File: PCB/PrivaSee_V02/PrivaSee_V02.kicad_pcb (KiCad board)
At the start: 4 copper layers, 69.8 x 90 mm, 31 parts, among them J1 RFPC-SMA27-F, J2 Batt_Solder_Point, J3 Conn_02x06_Odd_Even, SW1 Switch, SW2 SW_Push, U2 LM358, U3 254, U4 DFR0568, U6 ESP32-C5-DevKitC-1

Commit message: Fixed PCB Improt
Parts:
- moved G*** 3.64 mm to (84.5, 39.0)
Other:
- board text added: "Privasee"
- board text added: "V 1.0"
- board text added: "https://github.com/OSHE-Github/Privasee"

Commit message: Apply .gitignore to stop tracking ignored files
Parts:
- moved ? 2.55 mm to (85.0, 41.5)
- renumbered G*** to ?
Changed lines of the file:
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@@
 	(footprint "LOGO"
 		(layer "F.Cu")
-		(at 84.5 39)
-		(property "Reference" "G***"
+		(at 85 41.5)
+		(property "Reference" ""
 			(at 0 0 0)
 			(layer "F.SilkS")

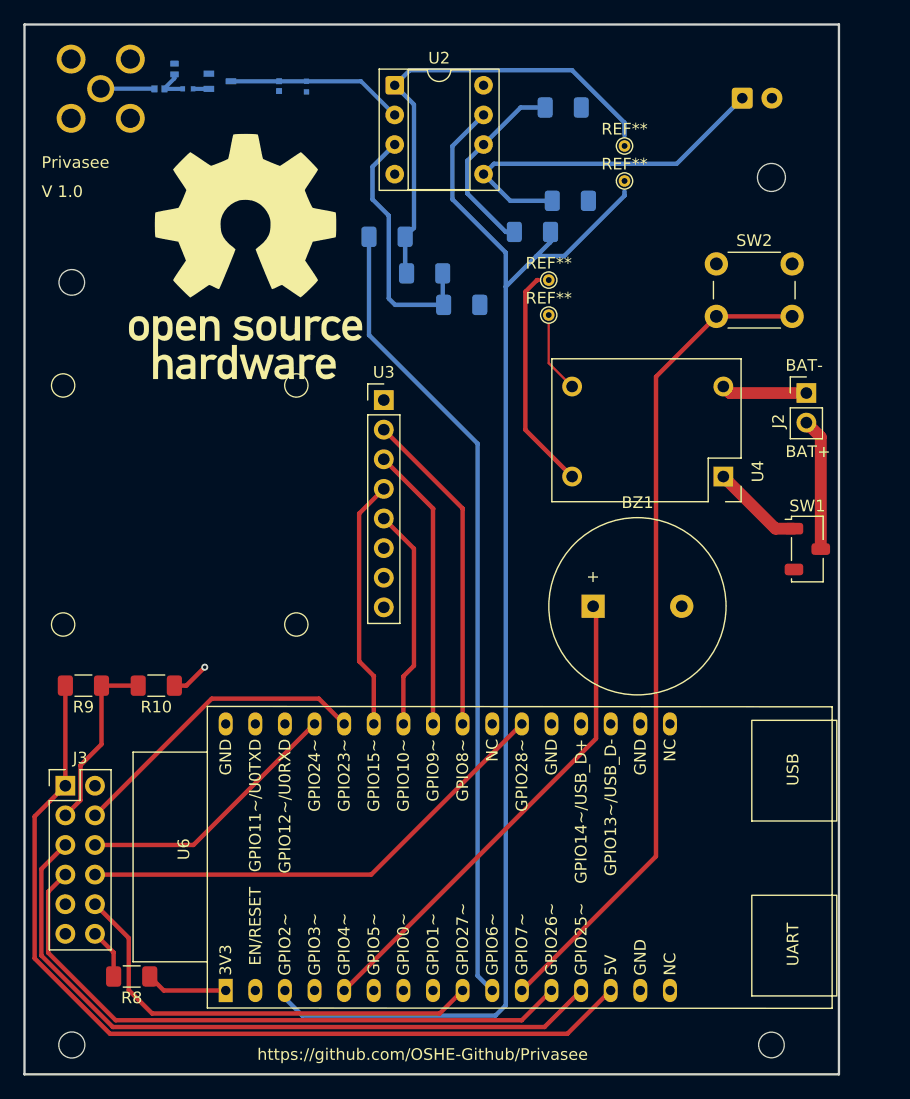
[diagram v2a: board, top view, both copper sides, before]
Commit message: PCB appearance updates
Updates to the silkscreen, footprint labels, and test points added
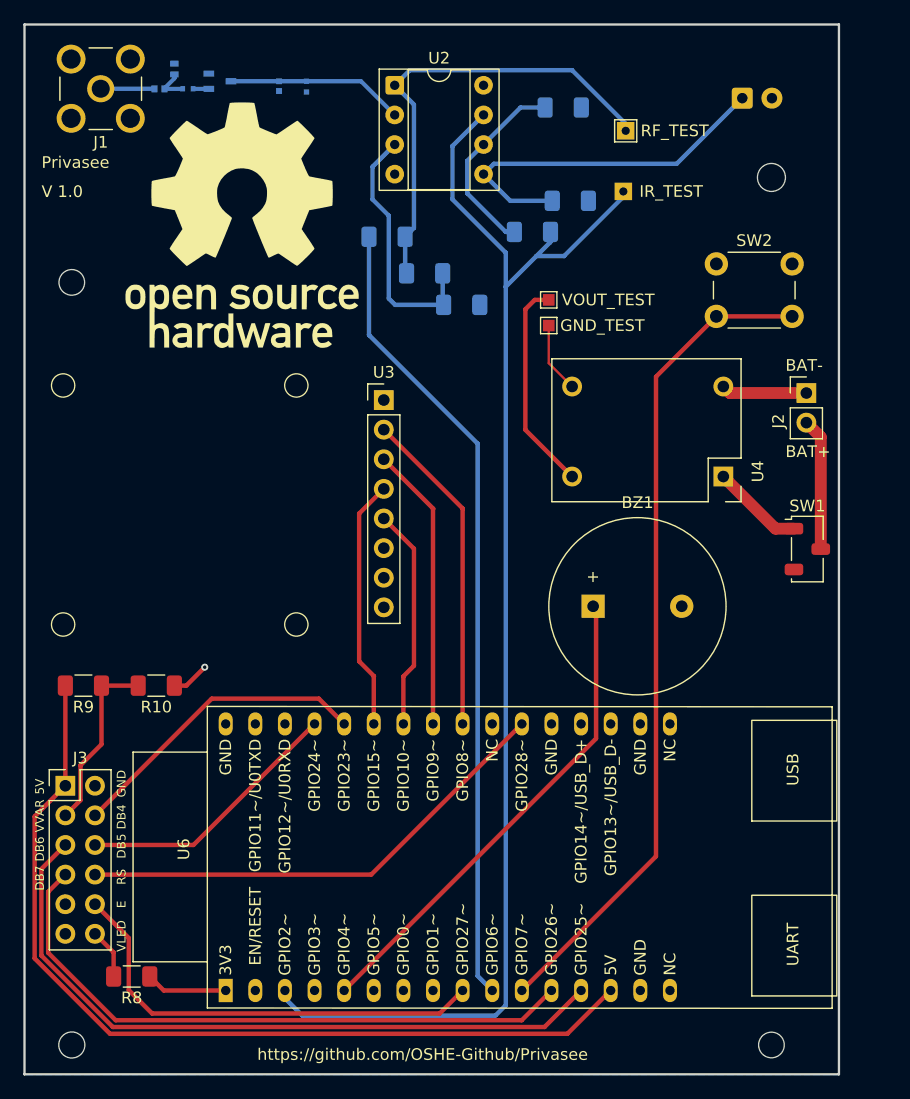
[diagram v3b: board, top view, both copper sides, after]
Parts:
- removed REF**: RF_TESTPOINT, TestPoint:TestPoint_THTPad_D1.0mm_Drill0.5mm
- removed REF**: GND_TESTPOINT, TestPoint:TestPoint_THTPad_D1.0mm_Drill0.5mm
- removed REF**: Vin_TESTPOINT, TestPoint:TestPoint_THTPad_D1.0mm_Drill0.5mm
- removed REF**: IR_TESTPOINT, TestPoint:TestPoint_THTPad_D1.0mm_Drill0.5mm
- added J4: VOUT_TEST, TestPoint:TestPoint_Pad_1.0x1.0mm, F.Cu at (111.0, 45.2)
- added J5: GND_TEST, TestPoint:TestPoint_Pad_1.0x1.0mm, F.Cu at (111.0, 47.4)
- added J6: IR_TEST, TestPoint:TestPoint_THTPad_1.5x1.5mm_Drill0.7mm, B.Cu at (117.4, 35.9)
- added J7: RF_TEST, TestPoint:TestPoint_THTPad_1.5x1.5mm_Drill0.7mm, F.Cu at (117.6, 30.7)
- J1: moved to F.Cu
- moved ? 2.72 mm to (84.7, 38.8)
- turned J1 to -90 degrees
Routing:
- net /3V3: track 140.6 -> 139.9 mm

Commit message: Stackup/RF Changes
Reassessed layer stackup. RF components are implemented/positioned correctly. Added values to passive RF components.
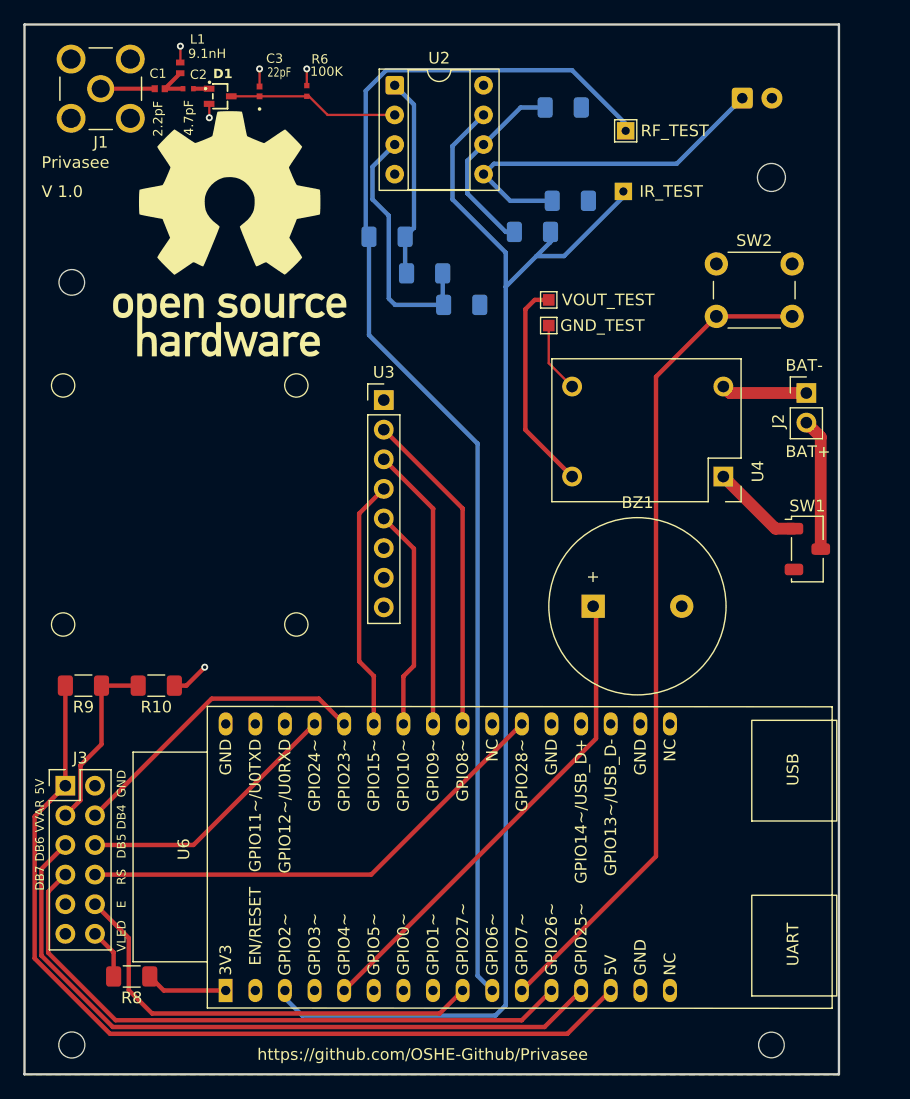
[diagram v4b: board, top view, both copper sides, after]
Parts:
- C1, C2, C3, D1, L1, R6: moved to F.Cu
- moved C3 1.73 mm to (86.2, 27.3), turned to 90 degrees
- moved ? 1.30 mm to (83.6, 39.5)
- moved D1 1.29 mm to (82.8, 27.7)
- moved L1 0.51 mm to (79.4, 25.3)
- moved R6 0.37 mm to (90.2, 27.3), turned to -90 degrees
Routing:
- net Net-(J7-Pin_1): track 69.0 -> 107.6 mm
- net Net-(R1-Pad2): track 40.4 -> 17.2 mm
- net GND: track 9.42 -> 15.0 mm, vias 1 -> 5
- net Net-(D1-C/A): track 15.5 -> 15.0 mm
- added copper zone on F.Cu, net (none)
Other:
- board text added: "100K"
- board text added: "2.2pF"
- board text added: "22pF"
- board text added: "4.7pF"
- board text added: "9.1nH"
- board text added: "D1"

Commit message: Removed Top Layer Ground Pour
I dont think this is needed and I think this may degrade signal performance for RF
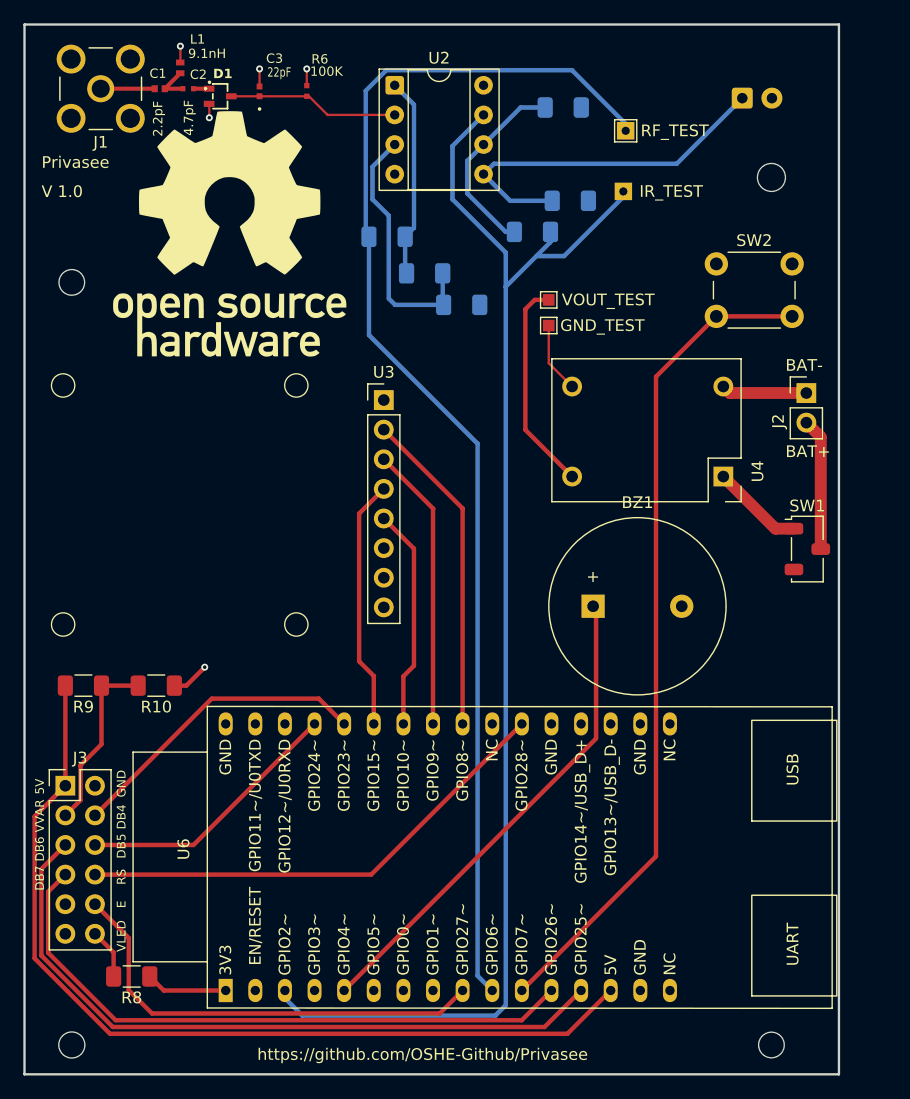
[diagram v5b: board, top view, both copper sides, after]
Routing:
- removed copper zone on F.Cu, net (none)
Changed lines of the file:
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@@
-	)
-	(zone
-		(layer "F.Cu")
-		(name "Signal")
-		(hatch edge 0.5)
-		(priority 1)
-		(connect_pads
-			(clearance 0.5)
-		)
-		(min_thickness 0.25)
-		(fill yes
-			(thermal_gap 0.5)
-			(thermal_bridge_width 0.5)
-			(island_removal_mode 1)
-		)
-		(polygon
-			(pts
-				(xy 135.89 21.59) (xy 135.89 111.64) (xy 66.04 111.63) (xy 66.04 21.59)
-			)
-		)
 	)
 	(zone

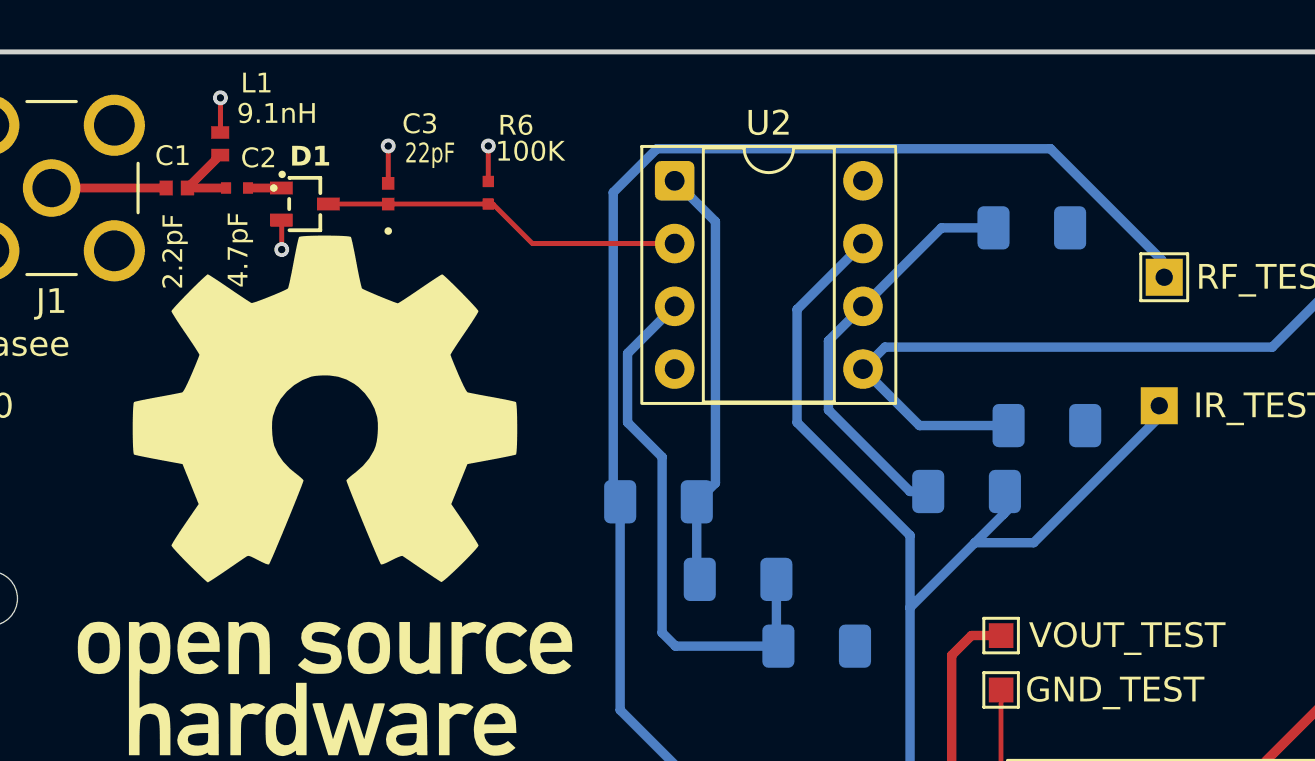
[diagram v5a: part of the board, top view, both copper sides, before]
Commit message: Minor Changes
Removed traces that are connected via 3v3 net. Removed acute angle at L1. Adjusted spacing near LM358 power.
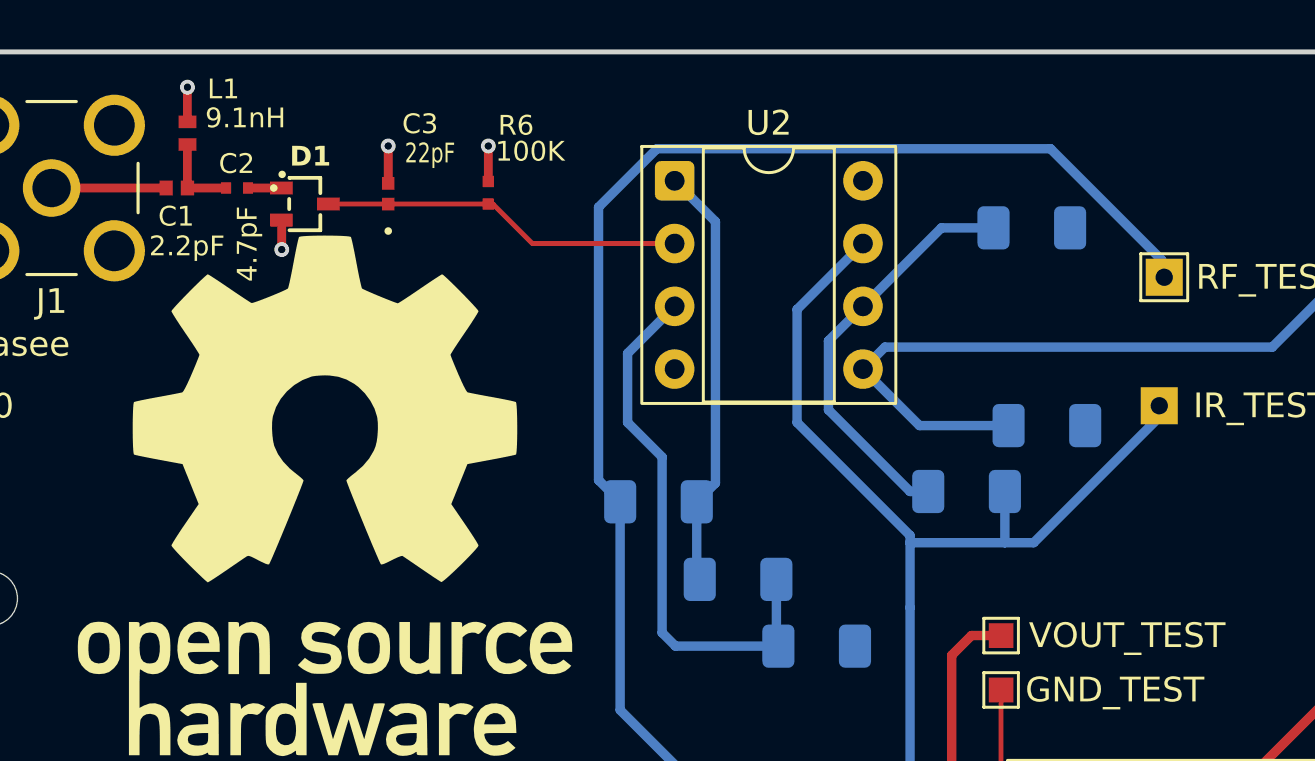
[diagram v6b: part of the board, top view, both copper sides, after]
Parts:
- moved L1 1.39 mm to (78.1, 24.9)
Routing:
- net /3V3: track 139.9 -> 25.4 mm
- net Net-(J6-Pin_1): track 116.5 -> 114.7 mm
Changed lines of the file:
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@@
 		(tags "GJM1555C1H4R7CB01D ")
 		(property "Reference" "C2"
-			(at -0.877216 1.2082 0)
+			(at 0.012784 0.9782 0)
 			(unlocked yes)
 			(layer "F.SilkS")
@@
 	(footprint "Snapeda:INDC1006X60N"
 		(layer "F.Cu")
-		(at 79.4 25.3 -90)
+		(at 78.075 24.87 -90)
 		(property "Reference" "L1"
-			(at -2.45 -1.48 0)
+			(at -1.78 -1.455 0)
 			(layer "F.SilkS")
 			(effects
@@
 		(at 77.643 27.0882 180)
 		(property "Reference" "C1"
-			(at 0.153 1.2982 180)
+			(at 0.023 -1.1518 180)
 			(layer "F.SilkS")
 			(effects
@@
 		)
 	)
-	(gr_text "9.1nH"
-		(at 80.07 24.55 0)
+	(gr_text "2.2pF"
+		(at 76.52 29.91 0)
 		(layer "F.SilkS")
 		(effects
@@
 		)
 	)
-	(gr_text "100K"
-		(at 90.53 26.08 0)
+	(gr_text "9.1nH"
+		(at 78.79 24.73 0)
 		(layer "F.SilkS")
 		(effects
@@
 		)
 	)
-	(gr_text "2.2pF"
-		(at 77.96 31.2 90)
+	(gr_text "100K"
+		(at 90.53 26.08 0)
 		(layer "F.SilkS")
 		(effects
@@
 	)
 	(gr_text "4.7pF"
-		(at 80.6 31.13 90)
+		(at 80.97 30.89 90)
 		(layer "F.SilkS")
 		(effects
@@
 	)
 	(segment
-		(start 78.075 27.085)
-		(end 79.4 25.76)
-		(width 0.355476)
-		(layer "F.Cu")
-		(net "Net-(C1-Pad1)")
-	)
-	(segment
 		(start 78.075 27.0882)
-		(end 79.638284 27.0882)
+		(end 78.075 25.33)
 		(width 0.355476)
 		(layer "F.Cu")
@@
 	(segment
 		(start 78.075 27.0882)
-		(end 78.075 27.085)
+		(end 79.638284 27.0882)
 		(width 0.355476)
 		(layer "F.Cu")
@@
 		(start 86.2 25.39)
 		(end 86.2 26.9)
-		(width 0.2)
+		(width 0.355476)
 		(layer "F.Cu")
 		(net "GND")
@@
 		(start 81.89 29.58)
 		(end 81.89 28.400916)
-		(width 0.2)
+		(width 0.355476)
 		(layer "F.Cu")
 		(net "GND")
@@
 	)
 	(segment
-		(start 79.41 24.83)
-		(end 79.4 24.84)
+		(start 78.08 24.4)
+		(end 78.07 24.41)
 		(width 0.2)
 		(layer "F.Cu")
@@
 		(start 90.25 25.39)
 		(end 90.25 26.8238)
-		(width 0.2)
+		(width 0.355476)
 		(layer "F.Cu")
 		(net "GND")
 	)
 	(segment
-		(start 79.41 23.44)
-		(end 79.41 24.83)
-		(width 0.2)
+		(start 78.075 23.01)
+		(end 78.075 24.4)
+		(width 0.355476)
 		(layer "F.Cu")
 		(net "GND")
@@
 	)
 	(via
-		(at 79.41 23.44)
+		(at 78.075 23.01)
 		(size 0.6)
 		(drill 0.3)
@@
 	)
 	(segment
-		(start 113.005 60.35)
-		(end 116.9 56.455)
-		(width 0.381)
-		(layer "In2.Cu")
-		(net "/3V3")
-	)
-	(segment
-		(start 113.005 60.35)
-		(end 109.9 63.455)
-		(width 0.381)
-		(layer "In2.Cu")
-		(net "/3V3")
-	)
-	(segment
-		(start 109.9 63.455)
-		(end 109.9 82.9)
-		(width 0.381)
-		(layer "In2.Cu")
-		(net "/3V3")
-	)
-	(segment
-		(start 116.9 56.455)
-		(end 116.9 53.527)
-		(width 0.381)
-		(layer "In2.Cu")
-		(net "/3V3")
-	)
-	(segment
-		(start 104.765496 82.957331)
-		(end 83.295996 104.426831)
-		(width 0.381)
-		(layer "In2.Cu")
-		(net "/3V3")
-	)
-	(segment
-		(start 104.3262 69.0288)
-		(end 96.8548 69.0288)
-		(width 0.381)
-		(layer "In2.Cu")
-		(net "/3V3")
-	)
-	(segment
 		(start 109.9 82.9)
 		(end 109.842669 82.957331)
@@
 	)
 	(segment
-		(start 116.9 53.527)
-		(end 97.79 34.417)
-		(width 0.381)
-		(layer "In2.Cu")
-		(net "/3V3")
-	)
-	(segment
-		(start 109.842669 82.957331)
-		(end 104.765496 82.957331)
-		(width 0.381)
-		(layer "In2.Cu")
-		(net "/3V3")
-	)
-	(segment
-		(start 113.005 60.35)
-		(end 104.3262 69.0288)
-		(width 0.381)
-		(layer "In2.Cu")
-		(net "/3V3")
-	)
-	(segment
 		(start 83.777244 27.7382)
 		(end 86.2 27.7382)
@@
 	)
 	(segment
-		(start 95.304 27.270268)
-		(end 95.304 39.505)
+		(start 104.902 103.172835)
+		(end 106.155996 104.426831)
 		(width 0.381)
 		(layer "B.Cu")
@@
 	)
 	(segment
-		(start 104.902 103.172835)
-		(end 106.155996 104.426831)
+		(start 95.585 39.786)
+		(end 95.585 48.214)
 		(width 0.381)
 		(layer "B.Cu")
@@
 	)
 	(segment
-		(start 95.585 39.786)
-		(end 95.585 48.214)
+		(start 94.71 27.864268)
+		(end 94.71 38.911)
 		(width 0.381)
 		(layer "B.Cu")
@@
 	)
 	(segment
-		(start 113 25.5)
-		(end 97.074268 25.5)
+		(start 117.5 30)
+		(end 113 25.5)
 		(width 0.381)
 		(layer "B.Cu")
@@
 	)
 	(segment
-		(start 104.902 57.531)
-		(end 104.902 103.172835)
+		(start 97.074268 25.5)
+		(end 94.71 27.864268)
 		(width 0.381)
 		(layer "B.Cu")
@@
 	)
 	(segment
-		(start 95.585 48.214)
-		(end 104.902 57.531)
+		(start 104.902 57.531)
+		(end 104.902 103.172835)
 		(width 0.381)
 		(layer "B.Cu")
@@
 	)
 	(segment
-		(start 113 25.5)
+		(start 117.5 31.1095)
 		(end 117.5 30)
 		(width 0.381)
@@
 	)
 	(segment
-		(start 95.304 39.505)
-		(end 95.585 39.786)
+		(start 95.585 48.214)
+		(end 104.902 57.531)
 		(width 0.381)
 		(layer "B.Cu")
@@
 	)
 	(segment
-		(start 117.5 30)
-		(end 117.5 31.1095)
+		(start 94.71 38.911)
+		(end 95.585 39.786)
 		(width 0.381)
 		(layer "B.Cu")
@@
 	)
 	(segment
-		(start 97.074268 25.5)
-		(end 95.304 27.270268)
+		(start 113 25.5)
+		(end 97.074268 25.5)
 		(width 0.381)
 		(layer "B.Cu")
@@
 	)
 	(segment
-		(start 107.315 44.069)
+		(start 107.315 41.44)
 		(end 107.315 41.148)
 		(width 0.381)
@@
 	)
 	(segment
-		(start 109.942 41.442)
-		(end 112.317358 41.442)
+		(start 107.315 44.069)
+		(end 107.315 41.44)
 		(width 0.381)
 		(layer "B.Cu")
@@
 	)
 	(segment
+		(start 111.15 41.442)
+		(end 107.317 41.442)
+		(width 0.381)
+		(layer "B.Cu")
+		(net "Net-(J6-Pin_1)")
+	)
+	(segment
+		(start 111.1516 41.4404)
+		(end 111.15 41.442)
+		(width 0.2)
+		(layer "B.Cu")
+		(net "Net-(J6-Pin_1)")
+	)
+	(segment
 		(start 88.375996 105.089196)
 		(end 88.375996 104.426831)
@@
 	)
 	(segment
+		(start 111.1516 39.37)
+		(end 111.1516 41.4404)
+		(width 0.381)
+		(layer "B.Cu")
+		(net "Net-(J6-Pin_1)")
+	)
+	(segment
 		(start 89.8652 106.5784)
 		(end 88.375996 105.089196)
@@
 	)
 	(segment
-		(start 111.252 40.132)
-		(end 111.0996 40.2844)
-		(width 0.381)
-		(layer "B.Cu")
-		(net "Net-(J6-Pin_1)")
-	)
-	(segment
-		(start 111.0996 40.2844)
-		(end 109.942 41.442)
-		(width 0.381)
-		(layer "B.Cu")
-		(net "Net-(J6-Pin_1)")
-	)
-	(segment
 		(start 107.315 41.148)
 		(end 102.743 36.576)
@@
 	)
 	(segment
-		(start 111.0996 39.422)
-		(end 111.1516 39.37)
-		(width 0.381)
-		(layer "B.Cu")
-		(net "Net-(J6-Pin_1)")
-	)
-	(segment
-		(start 109.942 41.442)
-		(end 107.315 44.069)
+		(start 107.317 41.442)
+		(end 107.315 41.44)
 		(width 0.381)
 		(layer "B.Cu")
@@
 	)
 	(segment
-		(start 111.0996 40.2844)
-		(end 111.0996 39.422)
+		(start 111.15 41.442)
+		(end 112.317358 41.442)
 		(width 0.381)
 		(layer "B.Cu")
